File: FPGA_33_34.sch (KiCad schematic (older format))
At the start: 6 parts, among them U1 XC7K160T-FFG676, U42 TXB0108PW

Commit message: clk switch power supply and general routing
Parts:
- added C316, C317: CC0201_100NF_6.3V_10%_X5R, CAPC0603X33N, symbol Capacitors_SMD:CC0201_100NF_6.3V_10%_X5R
- added R6: R0402_0R_JUMPER, Resistors SMD:RESC1005X40N, symbol Resistors_SMD:R0402_0R_JUMPER
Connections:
- net labels added: +3V3
- wire segments 195 -> 203

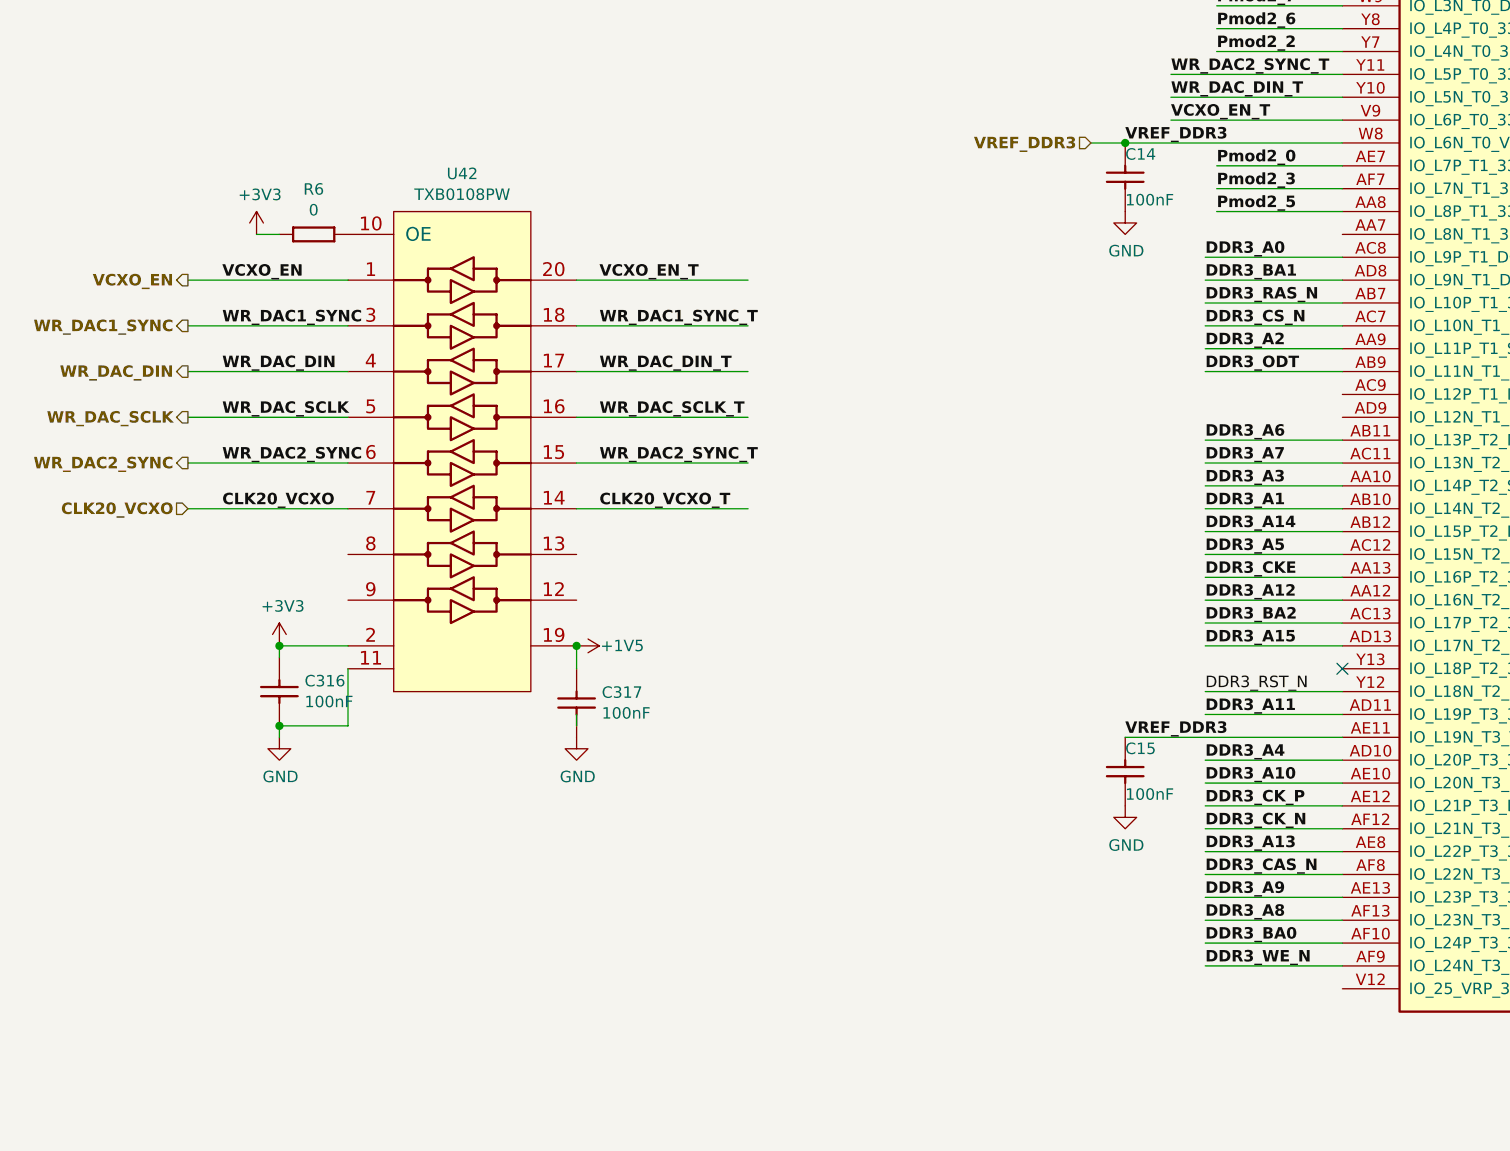
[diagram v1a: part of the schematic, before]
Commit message: DDR lenght mached, 2 additional LEDs added, I2C pullups voltage changed and other minor changes
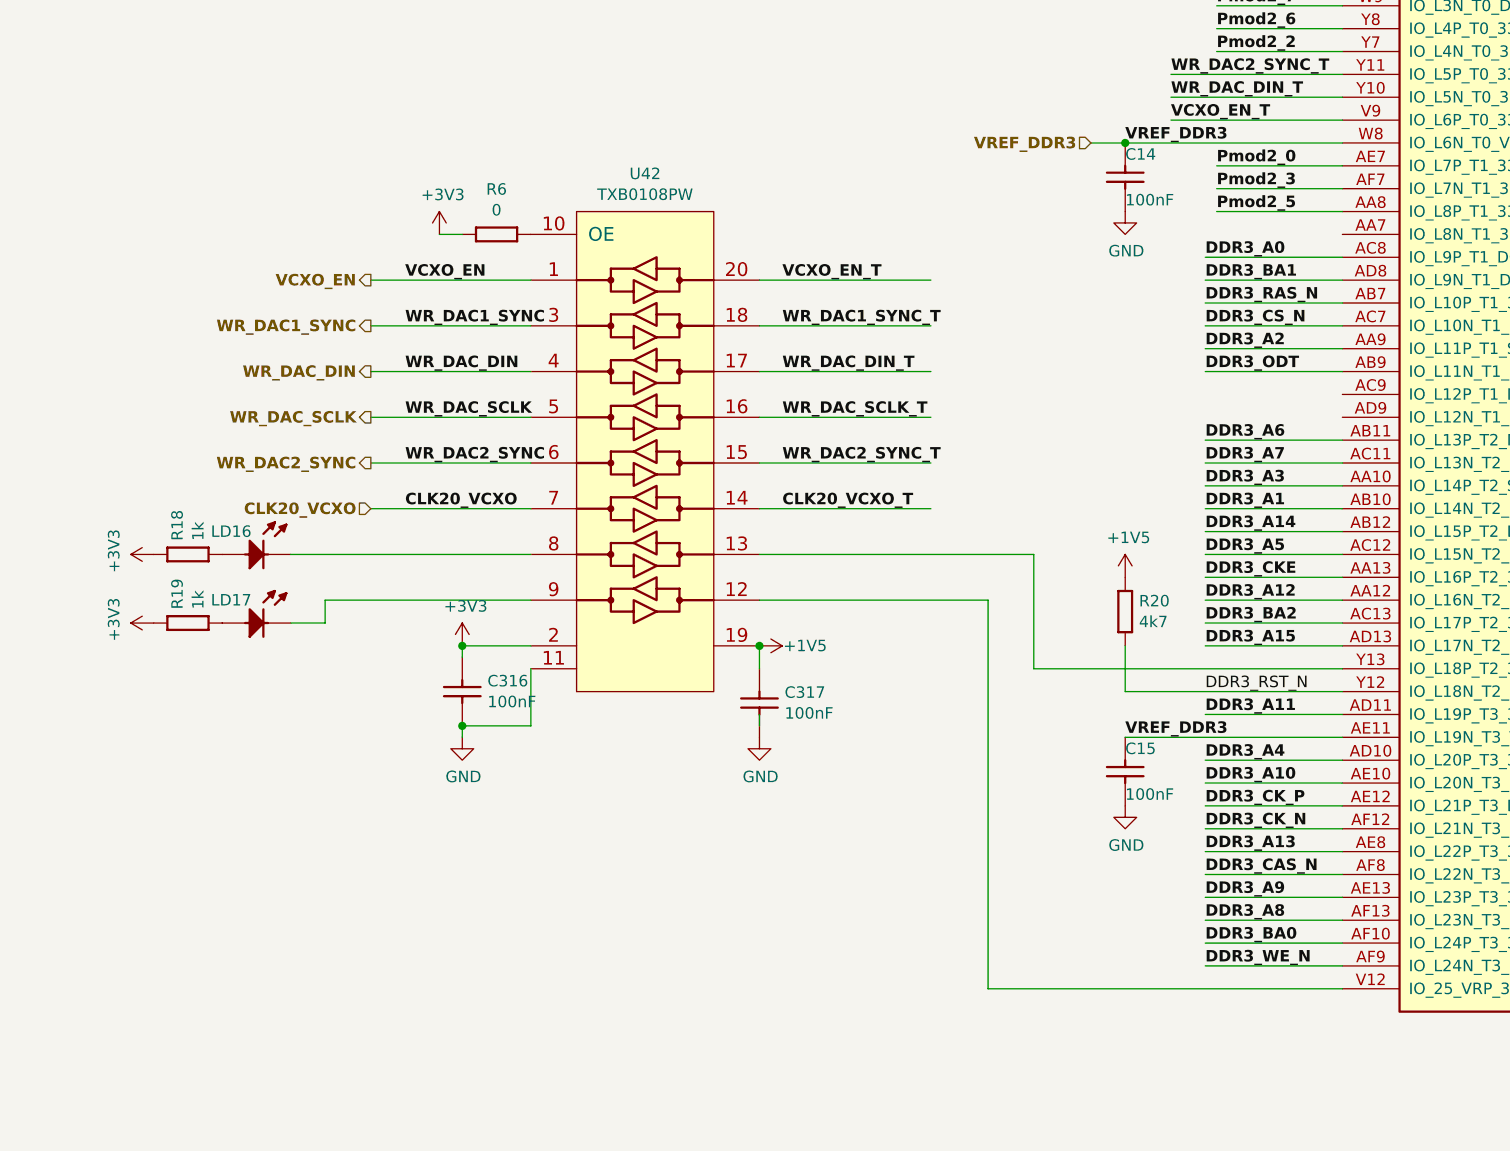
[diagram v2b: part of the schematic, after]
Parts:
- added LD16, LD17: LED_KINGBRIGHT_KPH-1608CGCK, ICs And Semiconductors SMD:LED_KINGBRIGHT_KPH-1608CGCK, symbol LEDs_&_Displays:LED_KINGBRIGHT_KPH-1608CGCK
- added R18, R19: R0402_1K_1%_0.0625W_100PPM, RESC1005X40N, symbol Resistors_SMD:R0402_1K_1%_0.0625W_100PPM
- added R20: R0402_4K7_1%_0.0625W_100PPM, RESC1005X40N, symbol Resistors_SMD:R0402_4K7_1%_0.0625W_100PPM
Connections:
- wire segments 203 -> 214
- no-connect marks 5 -> 4
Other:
- moved on the sheet: C316, C317, R6, U42

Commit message: REF CLK for MIG
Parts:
- added C379, C410: CC0201_100NF_6.3V_10%_X5R, CAPC0603X33N, symbol Capacitors_SMD:CC0201_100NF_6.3V_10%_X5R
- added R22, R23: R0201_100R_1%_0.05W_200PPM, RESC0603X28N, symbol Resistors_SMD:R0201_100R_1%_0.05W_200PPM
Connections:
- net labels added: DDR_REF_CLK_C_N, DDR_REF_CLK_C_P, DDR_REF_CLK_N, DDR_REF_CLK_P
- wire segments 214 -> 223
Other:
- moved on the sheet: C316, C317, LD16, LD17, R18, R19, R6, U42

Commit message: PN updated for some components, README_fab.txt updated
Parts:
- U1: value XC7K160T-FFG676 -> XC7K160T-2FFG676C
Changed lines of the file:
@@
 AR Path="/5C907554/5C721515/5DBE3995" Ref="U1"  Part="4"
 F 0 "U1" H 8350 1675 50  0000 C CNN
-F 1 "XC7K160T-FFG676" H 8350 1584 50  0000 C CNN
+F 1 "XC7K160T-2FFG676C" H 8350 1584 50  0000 C CNN
 F 2 "ICs And Semiconductors SMD_BGA:BGA676C100P26X26_2700X2700X260" H 8350 4650 50  0001 C CNN
 F 3 "" H 8350 4650 50  0000 C CNN
@@
 Text Label 5550 4950 0    50   ~ 10
 DDR_REF_CLK_C_N
-Wire Bus Line
-	14350 850  14350 1150
-Wire Bus Line
-	14350 4700 14350 5100
-Wire Bus Line
-	2050 2150 2050 2900
-Wire Bus Line
-	14350 1300 14350 2900
-Wire Bus Line
-	14350 5600 14350 8800
 $Comp
 L Capacitors_SMD:CC0201_100NF_6.3V_10%_X5R C?
@@
 	-1   0    0    1
 $EndComp
+Wire Bus Line
+	14350 850  14350 1150
+Wire Bus Line
+	14350 4700 14350 5100
+Wire Bus Line
+	2050 2150 2050 2900
+Wire Bus Line
+	14350 1300 14350 2900
+Wire Bus Line
+	14350 5600 14350 8800
 $EndSCHEMATC

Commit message: new PN for LEDs
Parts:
- LD16, LD17: Manufacturer Part Number KPH-1608CGCK -> 150060VS75000; Part Number LED_KINGBRIGHT_KPH-1608CGCK -> 150060VS75000
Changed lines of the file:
@@
 F 3 "" H 1600 6840 60  0001 L CNN
 F 4 "Green" H 1600 6750 60  0001 L CNN "Pole4"
-F 5 "LED_KINGBRIGHT_KPH-1608CGCK" H 1600 6750 60  0001 L CNN "Part Number"
+F 5 "150060VS75000" H 1600 6750 60  0001 L CNN "Part Number"
 F 6 "LED Green 1C 2A" H 1600 6660 60  0001 L CNN "Library Ref"
 F 7 "SchLib\\LEDs & Displays.SchLib" H 1600 6570 60  0001 L CNN "Library Path"
@@
 F 15 "SMD Green LED, Case 1.6mmX0.8mm(0603), 0.65mm Thickness" H 1600 5760 60  0001 L CNN "Part Description"
 F 16 "KINGBRIGHT" H 1600 5670 60  0001 L CNN "Manufacturer"
-F 17 "KPH-1608CGCK" H 1600 5580 60  0001 L CNN "Manufacturer Part Number"
+F 17 "150060VS75000" H 1600 5580 60  0001 L CNN "Manufacturer Part Number"
 F 18 "2" H 1600 5490 60  0001 L CNN "Pin Count"
 F 19 "~~" H 1600 5400 60  0001 L CNN "Case"
@@
 F 3 "" H 1600 7140 60  0001 L CNN
 F 4 "Green" H 1600 7050 60  0001 L CNN "Pole4"
-F 5 "LED_KINGBRIGHT_KPH-1608CGCK" H 1600 7050 60  0001 L CNN "Part Number"
+F 5 "150060VS75000" H 1600 7050 60  0001 L CNN "Part Number"
 F 6 "LED Green 1C 2A" H 1600 6960 60  0001 L CNN "Library Ref"
 F 7 "SchLib\\LEDs & Displays.SchLib" H 1600 6870 60  0001 L CNN "Library Path"
@@
 F 15 "SMD Green LED, Case 1.6mmX0.8mm(0603), 0.65mm Thickness" H 1600 6060 60  0001 L CNN "Part Description"
 F 16 "KINGBRIGHT" H 1600 5970 60  0001 L CNN "Manufacturer"
-F 17 "KPH-1608CGCK" H 1600 5880 60  0001 L CNN "Manufacturer Part Number"
+F 17 "150060VS75000" H 1600 5880 60  0001 L CNN "Manufacturer Part Number"
 F 18 "2" H 1600 5790 60  0001 L CNN "Pin Count"
 F 19 "~~" H 1600 5700 60  0001 L CNN "Case"

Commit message: Automated edit to move cache / rescue symbols to actual eeschem library
Results of running dissect_lib3.py, not posted here
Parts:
- U1: symbol FPGA_Xilinx_Kintex7:XC7K160T-FFG676 -> marble_misc:XC7K160T-FFG676
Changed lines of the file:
@@
 Connection ~ 6750 1750
 $Comp
-L FPGA_Xilinx_Kintex7:XC7K160T-FFG676 U?
+L marble_misc:XC7K160T-FFG676 U?
 U 4 1 5DBE3995
 P 8350 4650

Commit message: 16 warnings, 16 errors
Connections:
- no-connect marks 4 -> 6
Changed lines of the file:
@@
 	-1   0    0    1
 $EndComp
+NoConn ~ 6350 2550
+NoConn ~ 6350 4150
 Wire Bus Line
 	14350 850  14350 1150

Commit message: More consistent attributes for LEDs and BSS138
Should match Marble-Mini
Fewer complaints from KiBoM
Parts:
- LD16, LD17: Manufacturer KINGBRIGHT -> WURTH; Part Number 150060VS75000 -> LED_KINGBRIGHT_KPH-1608CGCK
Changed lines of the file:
@@
 F 3 "" H 1600 6840 60  0001 L CNN
 F 4 "Green" H 1600 6750 60  0001 L CNN "Pole4"
-F 5 "150060VS75000" H 1600 6750 60  0001 L CNN "Part Number"
+F 5 "LED_KINGBRIGHT_KPH-1608CGCK" H 1600 6750 60  0001 L CNN "Part Number"
 F 6 "LED Green 1C 2A" H 1600 6660 60  0001 L CNN "Library Ref"
 F 7 "SchLib\\LEDs & Displays.SchLib" H 1600 6570 60  0001 L CNN "Library Path"
@@
 F 14 "~~" H 1600 5850 60  0001 L CNN "Status"
 F 15 "SMD Green LED, Case 1.6mmX0.8mm(0603), 0.65mm Thickness" H 1600 5760 60  0001 L CNN "Part Description"
-F 16 "KINGBRIGHT" H 1600 5670 60  0001 L CNN "Manufacturer"
+F 16 "WURTH" H 1600 5670 60  0001 L CNN "Manufacturer"
 F 17 "150060VS75000" H 1600 5580 60  0001 L CNN "Manufacturer Part Number"
 F 18 "2" H 1600 5490 60  0001 L CNN "Pin Count"
@@
 F 3 "" H 1600 7140 60  0001 L CNN
 F 4 "Green" H 1600 7050 60  0001 L CNN "Pole4"
-F 5 "150060VS75000" H 1600 7050 60  0001 L CNN "Part Number"
+F 5 "LED_KINGBRIGHT_KPH-1608CGCK" H 1600 7050 60  0001 L CNN "Part Number"
 F 6 "LED Green 1C 2A" H 1600 6960 60  0001 L CNN "Library Ref"
 F 7 "SchLib\\LEDs & Displays.SchLib" H 1600 6870 60  0001 L CNN "Library Path"
@@
 F 14 "~~" H 1600 6150 60  0001 L CNN "Status"
 F 15 "SMD Green LED, Case 1.6mmX0.8mm(0603), 0.65mm Thickness" H 1600 6060 60  0001 L CNN "Part Description"
-F 16 "KINGBRIGHT" H 1600 5970 60  0001 L CNN "Manufacturer"
+F 16 "WURTH" H 1600 5970 60  0001 L CNN "Manufacturer"
 F 17 "150060VS75000" H 1600 5880 60  0001 L CNN "Manufacturer Part Number"
 F 18 "2" H 1600 5790 60  0001 L CNN "Pin Count"
